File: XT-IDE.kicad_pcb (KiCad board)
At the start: 2 copper layers, 114.3 x 106.7 mm, 46 parts, among them J1 CONN_3, J2 CONN_3, J3 CONN_2, J4 CONN_2, J5 INTERRUPT, P6 CONN_1, P7 CONN_1, SW1 I/O ADDR, SW2 ROM OPT, U1 74LS573, U10 74LS688, U11 74LS245, U2 74LS573, U3 74LS245, U4 74LS04, U5 74LS32, U6 74LS04, U7 74LS138, U8 74LS688, U9 28C256

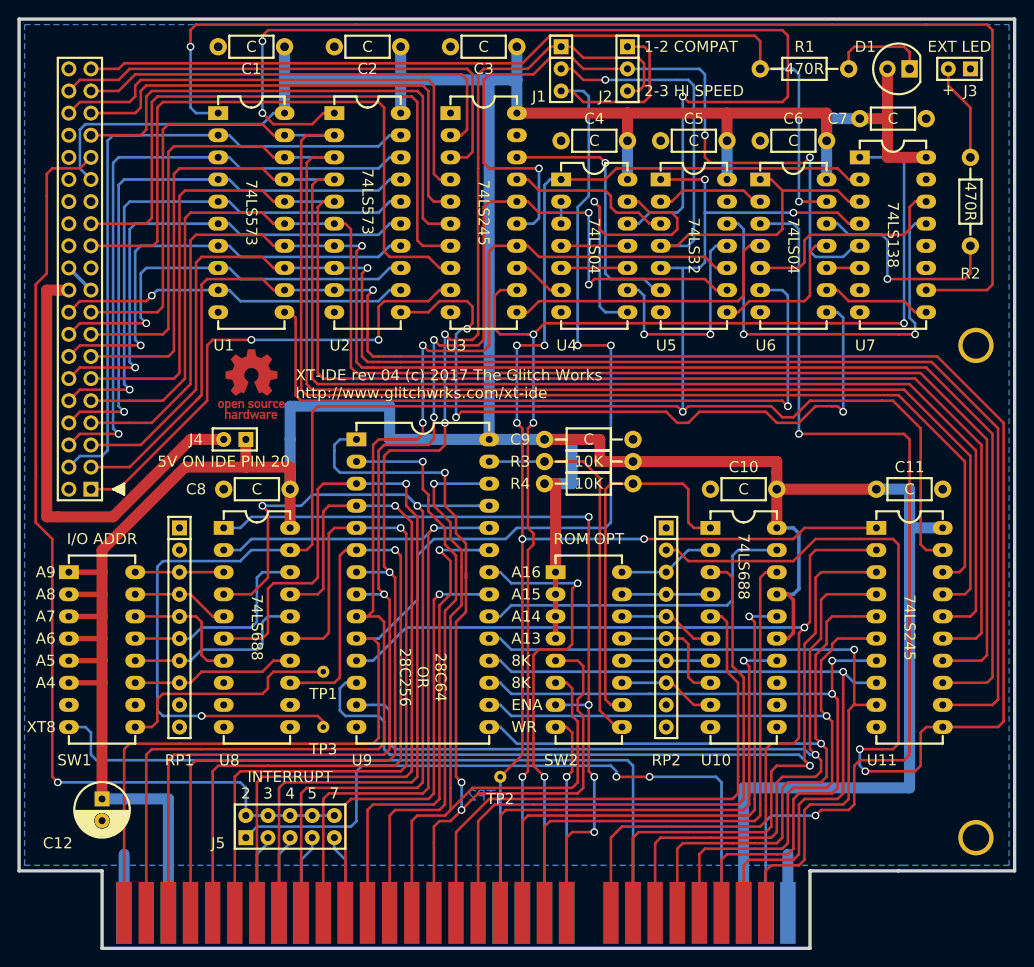
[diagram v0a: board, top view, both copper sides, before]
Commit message: Silk layer fixes.
Now showing calues of bypass caps and resistors
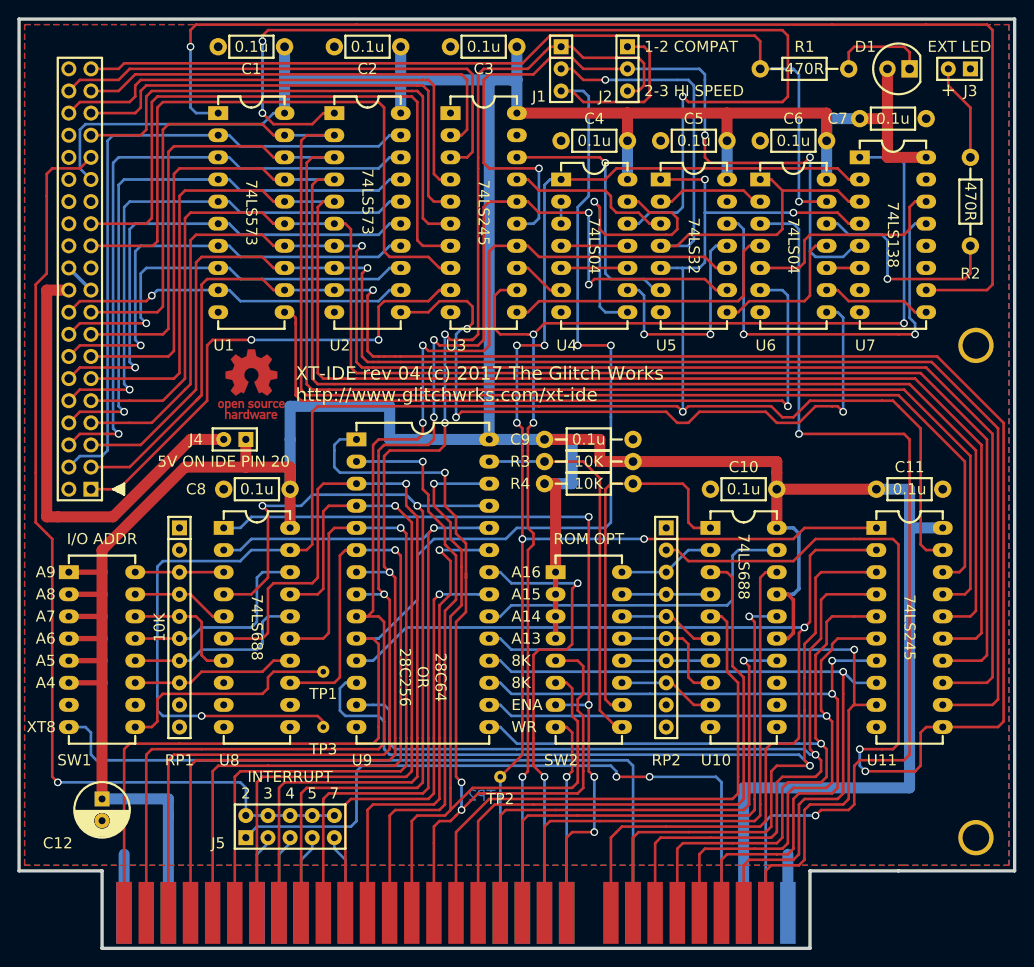
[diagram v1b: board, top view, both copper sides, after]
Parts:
- C1, C10, C11, C2, C3, C4, C5, C6, C7, C8, C9: value C -> 0.1u
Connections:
- IDE1 pad 21: /DMARQ -> (no net)
- IDE1 pad 27: /IORDY -> (no net)
- IDE1 pad 32: /IOCS16 -> (no net)
- IDE1 pad 34: /PDIAG -> (no net)
- RP1 pad 10: Net-(RP1-Pad10) -> (no net)
- RP1 pad 2: Net-(RP1-Pad2) -> (no net)
- RP1 pad 9: Net-(RP1-Pad9) -> (no net)
- RP2 pad 10: Net-(RP2-Pad10) -> (no net)
- RP2 pad 9: Net-(RP2-Pad9) -> (no net)
- SW1 pad 10: Net-(SW1-Pad10) -> (no net)
- SW1 pad 7: Net-(SW1-Pad7) -> (no net)
- U7 pad 11: Net-(U7-Pad11) -> (no net)
- U7 pad 12: Net-(U7-Pad12) -> (no net)
- U7 pad 15: Net-(U7-Pad15) -> (no net)
- U7 pad 7: Net-(U7-Pad7) -> (no net)
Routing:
- added copper zone on F.Cu, net GND

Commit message: Global solder mask and plot settings fixes
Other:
- rule pad_to_mask_clearance: 0.254 -> 0
